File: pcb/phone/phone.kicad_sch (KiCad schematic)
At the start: 0 parts

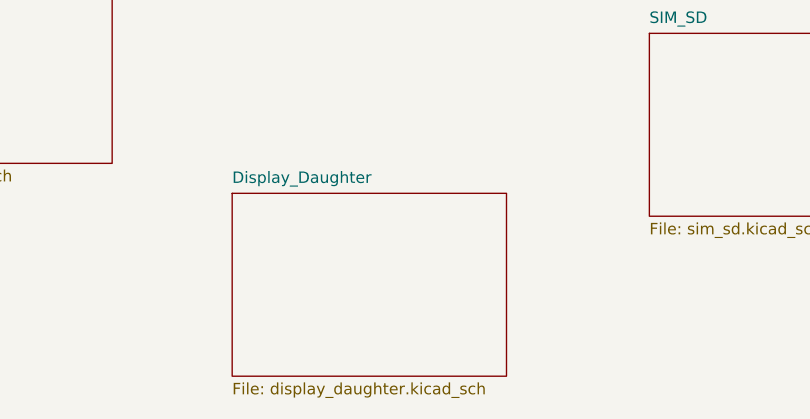
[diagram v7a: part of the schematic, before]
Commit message: Restructure display sheet for candybar + fix pinout + add backlight FET + power switch reversal
Display sheet (LOCKED):
- Fix J_DISP1 pinout to match HS20HS072RX datasheet (was 1/12 correct, now all 14 pins match)
- Add backlight FET circuit: Q1 (AO3400A), R20 (100ohm gate), R5 (10k pulldown), R19 moved to pin 10
- Fix R19 MPN: was 470ohm part with 4.7ohm value, swapped to RC0603JR-074R7L (correct 4.7ohm)
- Move display power from +1V8 to +3.3V (1.8V below VCC min 2.4V)
- Remove display_daughter sheet entry, J_HINGE1, J_HINGE2, OUTER_CS/OUTER_DC
- Add no-connect flags on MCU PG9/PG10 (freed from outer display)
- FPC connector orientation review flagged for PCB layout phase

Power switch (reversed 2026-08-27):
- Move SW21 from battery path back to TPS63021 EN pin (signal-level)
- Select C&K OS102011MA1QN1 (100mA SPDT, LCSC C226259), 8.4mm actuator, usable as finger toggle
- Battery always connected, charging while off restored
- Supersedes 2026-08-17 battery-path architecture

New library parts:
- ics:AO3400A (N-ch MOSFET, SOT-23, LCSC C20917)
- passives:0603WAF1000T5E (100ohm 0603, LCSC C22775)
- passives:RC0603JR-074R7L (4.7ohm 0603, LCSC C137621)
- electromech:OS102011MA1QN1 (SPDT slide switch, LCSC C226259)

Docs updated:
- project-log: 3 new entries (display review, power switch reversal, USB hub)
- bom.md: item 25b switch selected, display backlight parts
- block-diagram.md: +BATT net (no switch), U8 EN pin (switched by SW21)
- schematic-completion-plan.md: display sheet LOCKED, section F complete
- task-tracker.md: O2 updated with 2026-08-27 architecture
- ic-by-ic-review.md: Q3 superseded again, DEF-001 updated
- datasheets/README.md: HS20HS072RX pinout verified, SPI confirmed

Generated with [Devin](https://devin.ai)

Co-Authored-By: Devin <158243242+devin-ai-integration[bot]@users.noreply.github.com>
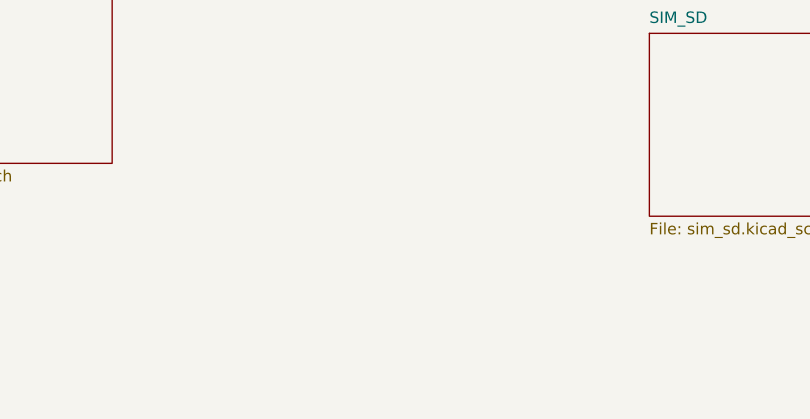
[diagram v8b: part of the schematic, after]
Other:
- removed sheet Display_Daughter
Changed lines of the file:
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@@
-	)
-	(sheet
-		(at 95.415 143.175)
-		(size 30.48 20.32)
-		(exclude_from_sim no)
-		(in_bom yes)
-		(on_board yes)
-		(dnp no)
-		(fields_autoplaced yes)
-		(stroke
-			(width 0.1524)
-			(type solid)
-		)
-		(fill
-			(color 0 0 0 0)
-		)
-		(property "Sheetname" "Display_Daughter"
-			(at 95.415 142.175 0)
-			(show_name no)
-			(do_not_autoplace no)
-			(effects
-				(font
-					(size 1.27 1.27)
-				)
-				(justify left bottom)
-			)
-		)
-		(property "Sheetfile" "display_daughter.kicad_sch"
-			(at 95.415 164.175 0)
-			(show_name no)
-			(do_not_autoplace no)
-			(effects
-				(font
-					(size 1.27 1.27)
-				)
-				(justify left top)
-			)
-		)
-		(instances
-			(project "phone"
-				(path "/451c3b43-1616-42cb-bf96-d436f4db82c2"
-					(page "6")
-				)
-			)
-		)
 	)
 	(sheet
